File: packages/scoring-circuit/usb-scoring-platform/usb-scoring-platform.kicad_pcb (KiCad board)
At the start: 4 copper layers, 160 x 100 mm, 187 parts, among them J1 GCT USB4105-GF-A, J10 5520250-2, J12 PD service: GND SDA SCL, J2 STM SWD 3.3V, J3 LEFT WEAPON A B C, J4 RIGHT WEAPON A B C, J5 PISTE - NOT protective earth, J6 ESP 3.3V UART recovery, J7 TST-108-02-G-D - HUB75, J8 645004114822 - panel 5V, J9 5520250-2, Q1 BSS138-7-F, Q2 BSS138-7-F, Q3 BSS138-7-F, Q4 BSS138, Q5 BSS138, SW1 STM RESET, SW2 ESP RESET, SW3 ESP BOOT, U1 STM32G474RET6, U10 SN74AXC1T45DCKR, U11 SN74AXC1T45DCKR, U12 WIZ850io, U13 TSOP38438, U14 SN74AHCT541PWR, U15 SN74AHCT541PWR, U16 4N32M, U17 4N32M, U18 LTM2884IY#PBF, U19 LMR36510ADDAR, U2 ESP32-S3-WROOM-1-N8R8, U20 TPS259470LRPWR, U3 TPD2E2U06DCKR, U4 AP2112K-3.3TRG1, U5 STUSB4500QTR, U6 REC30K-2405SZ, U7 AP63203WU-7, U8 74LVC125APW, U9 74LVC125APW, Y1 ABM3B-8.000MHZ-B2-T

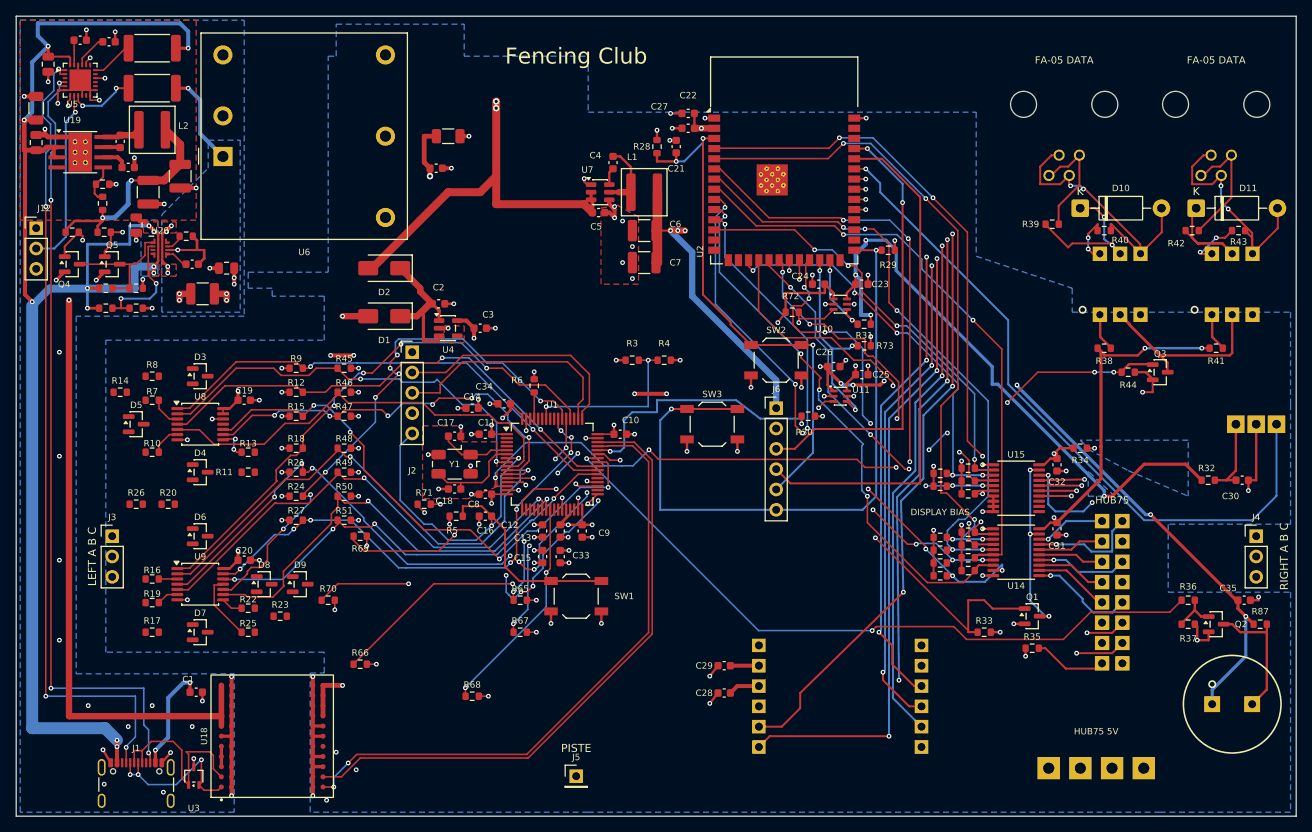
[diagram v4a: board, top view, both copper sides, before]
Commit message: feat(scoring-circuit): connect conductor harnesses and sense paths
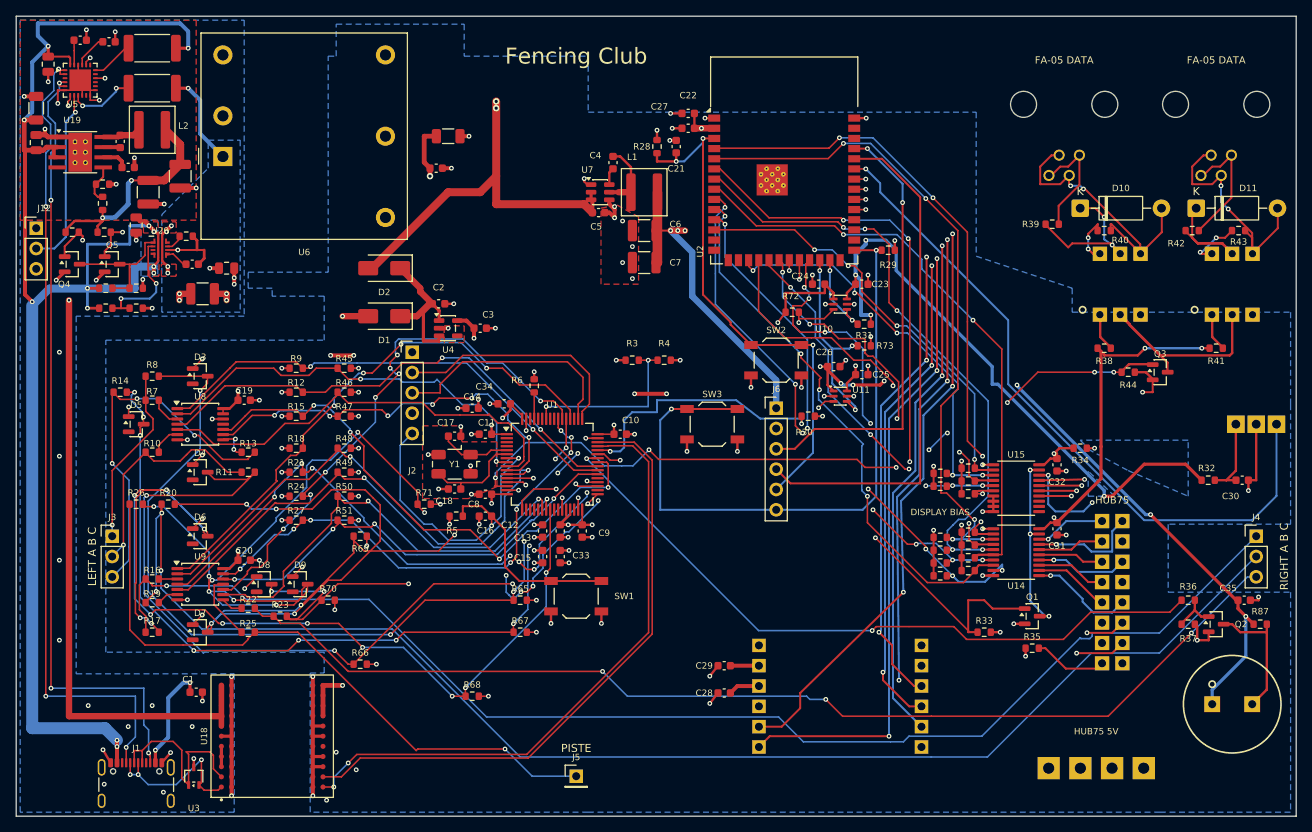
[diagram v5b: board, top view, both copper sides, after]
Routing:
- net RIGHT_B: track 0.00 -> 179.8 mm, vias 0 -> 3
- net RIGHT_A: track 0.00 -> 165.8 mm, vias 0 -> 1
- net RIGHT_C: track 0.00 -> 138.2 mm, vias 0 -> 3
- net RIGHT_A_SENSE: track 27.8 -> 130.6 mm, vias 2 -> 12
- net PISTE_SENSE: track 33.9 -> 119.9 mm, vias 5 -> 12
- net LEFT_A_SENSE: track 17.6 -> 103.5 mm, vias 3 -> 5
- net RIGHT_B_SENSE: track 38.8 -> 122.7 mm, vias 2 -> 7
- net PISTE: track 0.00 -> 80.7 mm, vias 0 -> 1
- net LEFT_C_SENSE: track 23.8 -> 101.9 mm, vias 3 -> 9
- net LEFT_B_SENSE: track 54.6 -> 118.7 mm, vias 2 -> 4
- net LEFT_C: track 0.00 -> 46.7 mm, vias 0 -> 3
- net LEFT_B: track 0.00 -> 29.1 mm, vias 0 -> 1
- net LEFT_A: track 0.00 -> 22.6 mm, vias 0 -> 1
- net RIGHT_C_SENSE: track 40.6 -> 60.1 mm, vias 2 -> 4
- net GND: track 153.7 -> 165.5 mm, vias 93 -> 100
